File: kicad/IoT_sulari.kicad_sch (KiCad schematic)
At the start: 19 parts, among them SW1 SW_SPST, U2 NRF9160-SICA-B1A-R

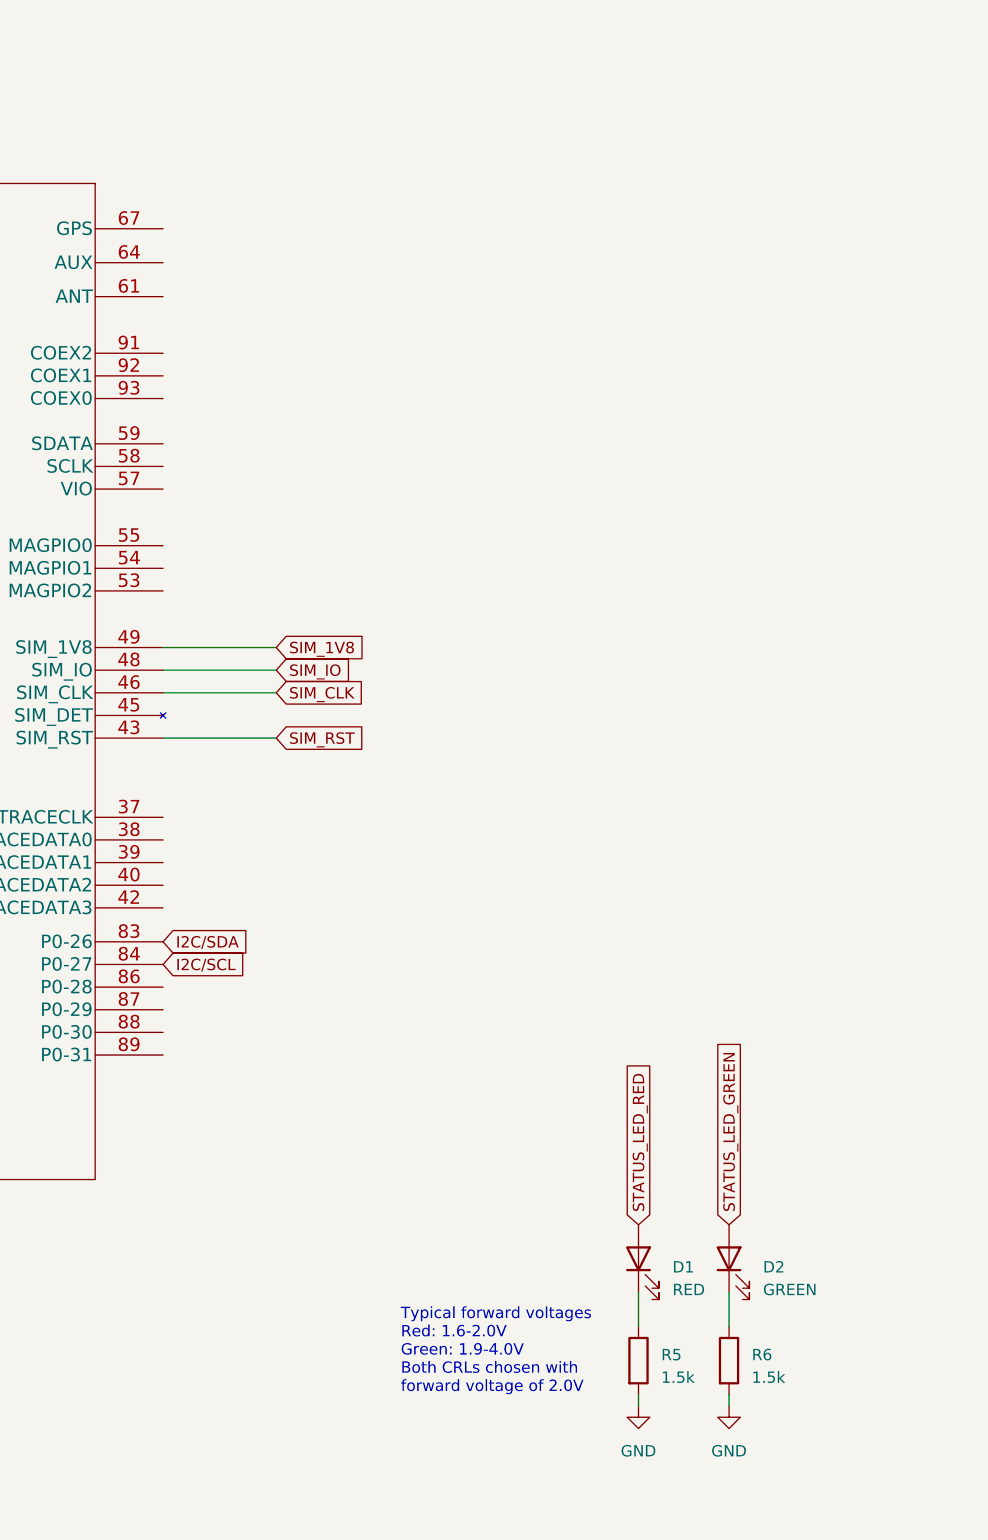
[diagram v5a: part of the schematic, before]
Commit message: Added Digikey part number and footprint to symbols, added signal TMP_ALERT
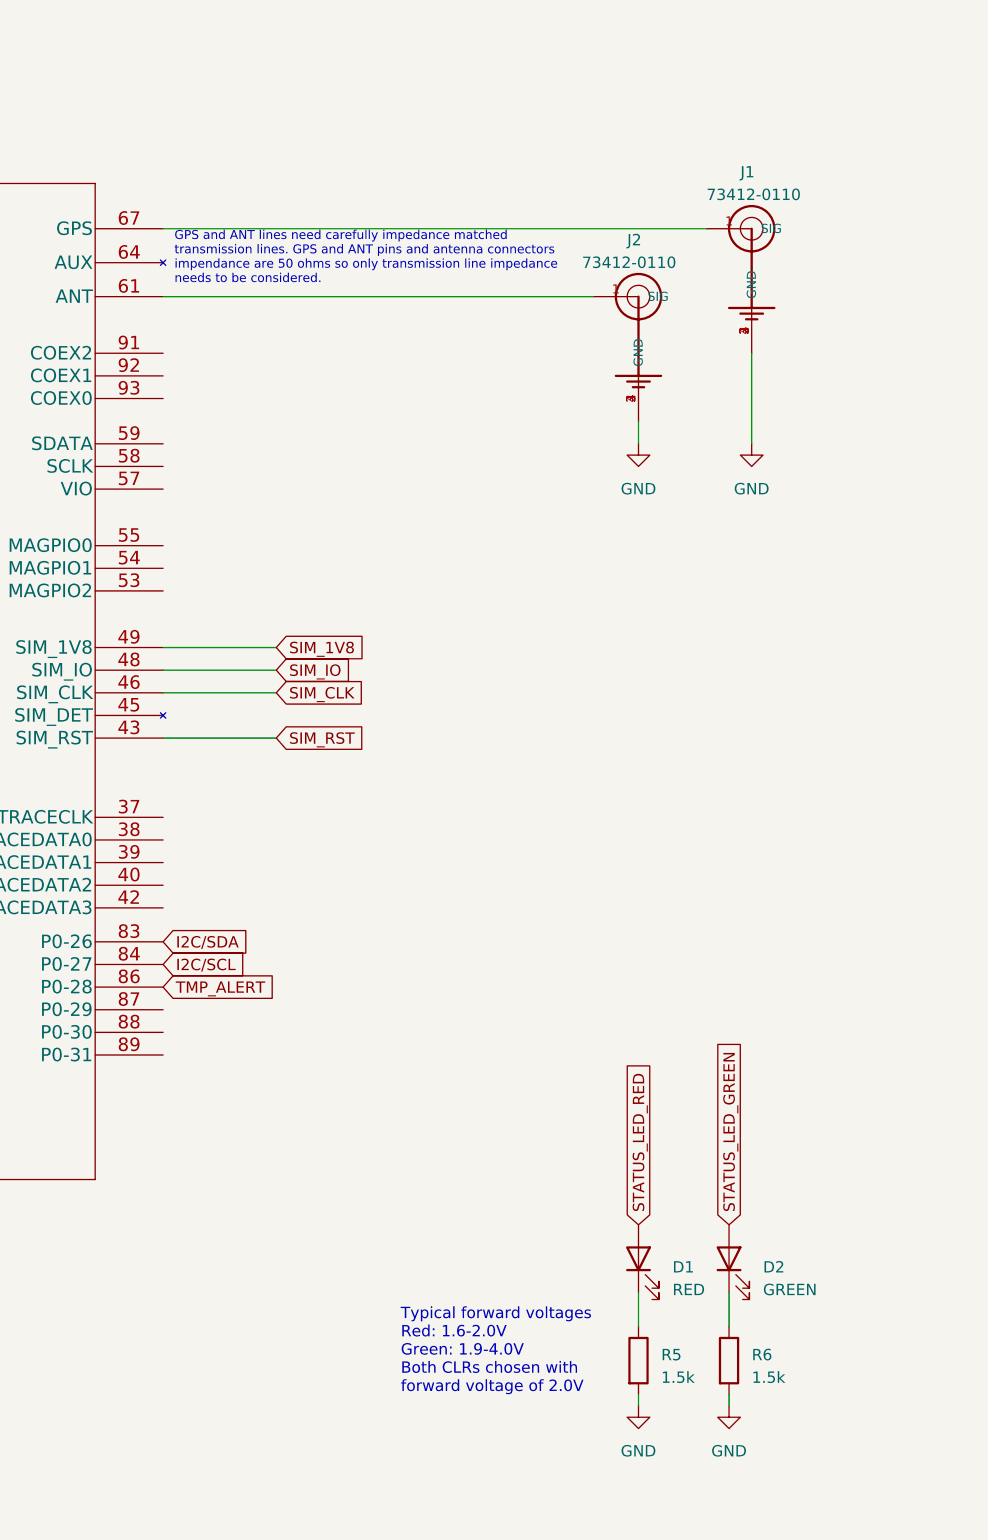
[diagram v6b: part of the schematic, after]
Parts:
- added J1, J2: 73412-0110, 73412-0110:MOLEX_73412-0110, symbol 73412-0110:73412-0110
- U2: footprint LGA_16X10P5_NOR -> NRF-9160-SICA-B1A-R:NRF9160-SICA-B1A-R; Digikey (none) -> 4823-NRF9160-SICA-B1A-RCT-ND
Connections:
- net GND: now also J1.2 (GND), J1.3 (GND), J1.4 (GND), J2.2 (GND), J2.3 (GND), J2.4 (GND)
- net at U2.61 (ANT): now also J2.1 (SIG)
- net at U2.67 (GPS): now also J1.1 (SIG)
- net TMP_ALERT: now reaches U2.86 (P0-28)
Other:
- note added: "GPS and ANT lines need carefully impedance matched transmission lines. GPS and ANT pins and antenna connectors impendance are 50 ohms so only transmission line impedance needs to be considered."
- note added: "Typical forward voltages Red: 1.6-2.0V Green: 1.9-4.0V Both CLRs chosen with forward voltage of 2.0V"
- note removed: "Typical forward voltages Red: 1.6-2.0V Green: 1.9-4.0V Both CRLs chosen with forward voltage of 2.0V"
- title: IoT sensor -> nRF9160 based IoT sensor
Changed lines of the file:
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@@
   (paper "A4")
   (title_block
-    (title "IoT sensor")
+    (title "nRF9160 based IoT sensor")
     (company "University of Oulu")
   )
@@
     (stroke (width 0) (type default))
   )
+  (wire (pts (xy 275.59 40.64) (xy 275.59 50.8))
+    (stroke (width 0) (type default))
+  )
   (wire (pts (xy 20.32 93.98) (xy 20.32 91.44))
     (stroke (width 0) (type default))
@@
     (stroke (width 0) (type default))
   )
+  (wire (pts (xy 262.89 48.26) (xy 262.89 50.8))
+    (stroke (width 0) (type default))
+  )
   (wire (pts (xy 20.32 109.22) (xy 20.32 106.68))
     (stroke (width 0) (type default))
@@
     (stroke (width 0) (type default))
   )
+  (wire (pts (xy 209.55 26.67) (xy 270.51 26.67))
+    (stroke (width 0) (type default))
+  )
   (wire (pts (xy 93.98 33.02) (xy 93.98 35.56))
     (stroke (width 0) (type default))
@@
   )
   (wire (pts (xy 20.32 129.54) (xy 25.4 129.54))
+    (stroke (width 0) (type default))
+  )
+  (wire (pts (xy 209.55 34.29) (xy 257.81 34.29))
     (stroke (width 0) (type default))
   )
@@
     (effects (font (size 1.27 1.27)) (justify left bottom))
   )
-  (text "Typical forward voltages\nRed: 1.6-2.0V\nGreen: 1.9-4.0V\nBoth CRLs chosen with\nforward voltage of 2.0V"
+  (text "GPS and ANT lines need carefully impedance matched \ntransmission lines. GPS and ANT pins and antenna connectors\nimpendance are 50 ohms so only transmission line impedance\nneeds to be considered."
+    (at 210.82 33.02 0)
+    (effects (font (size 1 1)) (justify left bottom))
+  )
+  (text "Typical forward voltages\nRed: 1.6-2.0V\nGreen: 1.9-4.0V\nBoth CLRs chosen with\nforward voltage of 2.0V"
     (at 236.22 157.48 0)
     (effects (font (size 1.27 1.27)) (justify left bottom))
@@
     )
   )
+  (global_label "TMP_ALERT" (shape input) (at 209.55 111.76 0) (fields_autoplaced)
+    (effects (font (size 1.27 1.27)) (justify left))
+    (property "Intersheetrefs" "${INTERSHEET_REFS}" (at 222.6157 111.76 0)
+      (effects (font (size 1.27 1.27)) (justify left) hide)
+    )
+  )
   (global_label "SIM_RST" (shape input) (at 222.25 83.82 0) (fields_autoplaced)
     (effects (font (size 1.27 1.27)) (justify left))
@@
       (effects (font (size 1.524 1.524)))
     )
-    (property "Footprint" "LGA_16X10P5_NOR" (at 175.26 17.78 0)
+    (property "Footprint" "NRF-9160-SICA-B1A-R:NRF9160-SICA-B1A-R" (at 175.26 17.78 0)
       (effects (font (size 1.524 1.524)) hide)
     )
     (property "Datasheet" "" (at 147.32 33.02 0)
       (effects (font (size 1.524 1.524)))
+    )
+    (property "Digikey" "4823-NRF9160-SICA-B1A-RCT-ND" (at 130.81 19.05 0)
+      (effects (font (size 1.27 1.27)) hide)
     )
     (pin "100")
@@
     )
   )
+  (symbol (lib_id "power:GND") (at 262.89 50.8 0) (unit 1)
+    (in_bom yes) (on_board yes) (dnp no) (fields_autoplaced)
+    (property "Reference" "#PWR027" (at 262.89 57.15 0)
+      (effects (font (size 1.27 1.27)) hide)
+    )
+    (property "Value" "GND" (at 262.89 55.88 0)
+      (effects (font (size 1.27 1.27)))
+    )
+    (property "Footprint" "" (at 262.89 50.8 0)
+      (effects (font (size 1.27 1.27)) hide)
+    )
+    (property "Datasheet" "" (at 262.89 50.8 0)
+      (effects (font (size 1.27 1.27)) hide)
+    )
+    (pin "1")
+    (instances
+      (project "IoT_sulari"
+        (path "/184b47ed-2c2b-4c02-be35-d18f4f4e5685"
+          (reference "#PWR027") (unit 1)
+        )
+      )
+    )
+  )
   (symbol (lib_id "Device:C") (at 110.49 39.37 0) (unit 1)
     (in_bom yes) (on_board yes) (dnp no) (fields_autoplaced)
@@
         (path "/184b47ed-2c2b-4c02-be35-d18f4f4e5685"
           (reference "C6") (unit 1)
+        )
+      )
+    )
+  )
+  (symbol (lib_id "73412-0110:73412-0110") (at 262.89 34.29 0) (mirror y) (unit 1)
+    (in_bom yes) (on_board yes) (dnp no)
+    (property "Reference" "J2" (at 261.62 27.94 0)
+      (effects (font (size 1.27 1.27)) (justify right))
+    )
+    (property "Value" "73412-0110" (at 256.54 30.48 0)
+      (effects (font (size 1.27 1.27)) (justify right))
+    )
+    (property "Footprint" "73412-0110:MOLEX_73412-0110" (at 262.89 34.29 0)
+      (effects (font (size 1.27 1.27)) (justify bottom) hide)
+    )
+    (property "Datasheet" "" (at 262.89 34.29 0)
+      (effects (font (size 1.27 1.27)) hide)
+    )
+    (property "MANUFACTURER" "Molex" (at 262.89 34.29 0)
+      (effects (font (size 1.27 1.27)) (justify bottom) hide)
+    )
+    (property "Digikey" "WM5587CT-ND" (at 262.89 34.29 0)
+      (effects (font (size 1.27 1.27)) hide)
+    )
+    (pin "1")
+    (pin "2")
+    (pin "3")
+    (pin "4")
+    (instances
+      (project "IoT_sulari"
+        (path "/184b47ed-2c2b-4c02-be35-d18f4f4e5685"
+          (reference "J2") (unit 1)
         )
       )
@@
       (effects (font (size 1.524 1.524)))
     )
-    (property "Footprint" "LGA_16X10P5_NOR" (at 54.61 73.66 0)
+    (property "Footprint" "NRF-9160-SICA-B1A-R:NRF9160-SICA-B1A-R" (at 54.61 73.66 0)
       (effects (font (size 1.524 1.524)) hide)
     )
     (property "Datasheet" "" (at 26.67 88.9 0)
       (effects (font (size 1.524 1.524)))
+    )
+    (property "Digikey" "4823-NRF9160-SICA-B1A-RCT-ND" (at 10.16 74.93 0)
+      (effects (font (size 1.27 1.27)) hide)
     )
     (pin "100")
@@
     )
   )
+  (symbol (lib_id "73412-0110:73412-0110") (at 275.59 26.67 0) (mirror y) (unit 1)
+    (in_bom yes) (on_board yes) (dnp no)
+    (property "Reference" "J1" (at 274.32 20.32 0)
+      (effects (font (size 1.27 1.27)) (justify right))
+    )
+    (property "Value" "73412-0110" (at 270.51 22.86 0)
+      (effects (font (size 1.27 1.27)) (justify right))
+    )
+    (property "Footprint" "73412-0110:MOLEX_73412-0110" (at 275.59 26.67 0)
+      (effects (font (size 1.27 1.27)) (justify bottom) hide)
+    )
+    (property "Datasheet" "" (at 275.59 26.67 0)
+      (effects (font (size 1.27 1.27)) hide)
+    )
+    (property "MANUFACTURER" "Molex" (at 275.59 26.67 0)
+      (effects (font (size 1.27 1.27)) (justify bottom) hide)
+    )
+    (property "Digikey" "WM5587CT-ND" (at 275.59 26.67 0)
+      (effects (font (size 1.27 1.27)) hide)
+    )
+    (pin "1")
+    (pin "2")
+    (pin "3")
+    (pin "4")
+    (instances
+      (project "IoT_sulari"
+        (path "/184b47ed-2c2b-4c02-be35-d18f4f4e5685"
+          (reference "J1") (unit 1)
+        )
+      )
+    )
+  )
   (symbol (lib_id "power:GND") (at 135.89 135.89 0) (unit 1)
     (in_bom yes) (on_board yes) (dnp no) (fields_autoplaced)
@@
         )
       )
+    )
+  )
+  (symbol (lib_id "power:GND") (at 275.59 50.8 0) (unit 1)
+    (in_bom yes) (on_board yes) (dnp no) (fields_autoplaced)
+    (property "Reference" "#PWR026" (at 275.59 57.15 0)
+      (effects (font (size 1.27 1.27)) hide)
+    )
+    (property "Value" "GND" (at 275.59 55.88 0)
+      (effects (font (size 1.27 1.27)))
+    )
+    (property "Footprint" "" (at 275.59 50.8 0)
+      (effects (font (size 1.27 1.27)) hide)
+    )
+    (property "Datasheet" "" (at 275.59 50.8 0)
+      (effects (font (size 1.27 1.27)) hide)
+    )
+    (pin "1")
+    (instances
+      (project "IoT_sulari"
+        (path "/184b47ed-2c2b-4c02-be35-d18f4f4e5685"
+          (reference "#PWR026") (unit 1)
+        )
+      )
